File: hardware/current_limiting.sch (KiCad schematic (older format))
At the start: 3 parts, among them U7 MT9700

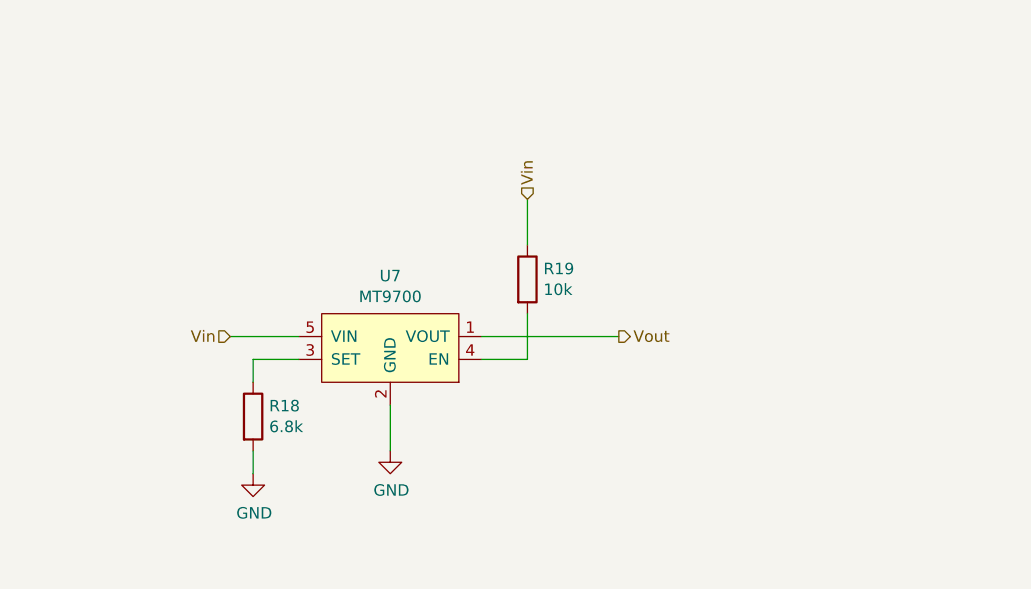
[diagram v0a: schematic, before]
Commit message: Changed to pure-serial topology. Changed to beefier mcu.
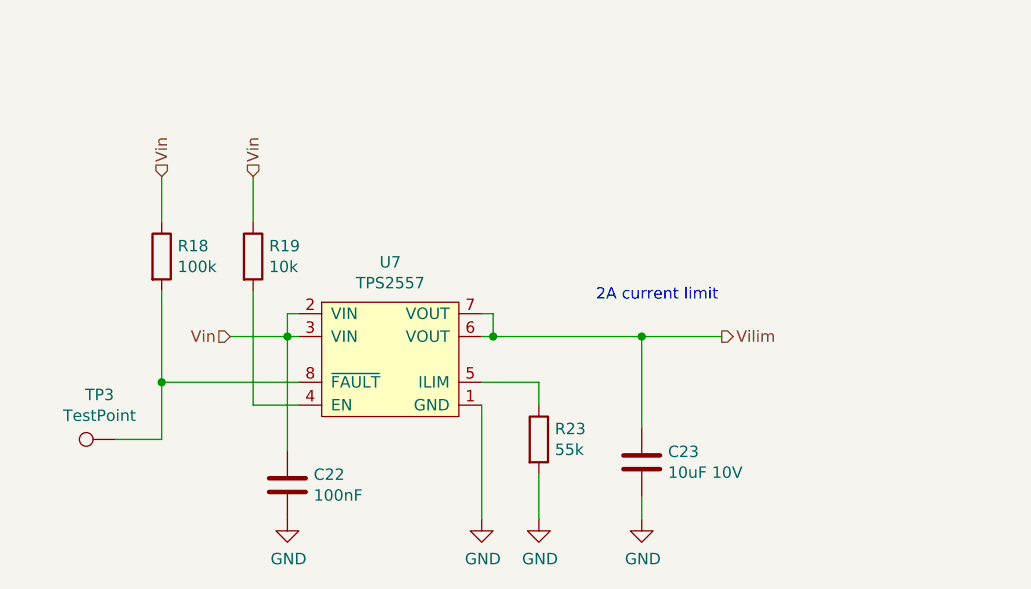
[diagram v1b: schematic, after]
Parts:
- removed U7: MT9700, Package_TO_SOT_SMD:SOT-23-5_HandSoldering, symbol pi-supercap-ups:MT9700
- added C22: 100nF, symbol Device:C
- added C23: 10uF 10V, symbol Device:C
- added R23: 55k, Resistor_SMD:R_0603_1608Metric_Pad1.05x0.95mm_HandSolder, symbol Device:R
- added TP3: TestPoint, symbol Connector:TestPoint
- added U7: TPS2557, symbol pi-supercap-ups:TPS2557
- R18: value 6.8k -> 100k
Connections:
- net GND: now also C22.2, C23.2, R23.2, U7.1 (GND); no longer R18.2
- net Vin: now also R18.1, C22.1, U7.2 (VIN), U7.3 (VIN)
- net at R19.2: now also U7.4 (EN)
- new net: R18.2, TP3.1, U7.8 (~FAULT)
- new net: R23.1, U7.5 (ILIM)
- new net Vilim: C23.1, U7.6 (VOUT), U7.7 (VOUT)
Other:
- note added: "2A current limit"
- moved on the sheet: R18, R19
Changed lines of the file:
@@
-EESchema Schematic File Version 4
+EESchema Schematic File Version 5
 LIBS:pi-supercap-ups-cache
-EELAYER 26 0
+EELAYER 30 0
 EELAYER END
 $Descr A4 11693 8268
 encoding utf-8
-Sheet 8 8
+Sheet 7 8
 Title ""
 Date ""
@@
 Comment4 ""
 $EndDescr
-$Comp
-L pi-supercap-ups:MT9700 U7
-U 1 1 5CA93FCA
-P 3000 2050
-F 0 "U7" H 3000 2365 50  0000 C CNN
-F 1 "MT9700" H 3000 2274 50  0000 C CNN
-F 2 "Package_TO_SOT_SMD:SOT-23-5_HandSoldering" H 3000 2250 50  0001 C CNN
-F 3 "" H 3000 2250 50  0001 C CNN
-	1    3000 2050
-	1    0    0    -1
-$EndComp
 Text HLabel 2300 2000 0    50   Input ~ 0
 Vin
-Text HLabel 4000 2000 2    50   Output ~ 0
-Vout
+Text HLabel 4450 2000 2    50   Output ~ 0
+Vilim
 $Comp
 L Device:R R18
 U 1 1 5CA94123
-P 2400 2350
-F 0 "R18" H 2470 2396 50  0000 L CNN
-F 1 "6.8k" H 2470 2305 50  0000 L CNN
-F 2 "Resistor_SMD:R_0603_1608Metric_Pad1.05x0.95mm_HandSolder" V 2330 2350 50  0001 C CNN
-F 3 "~" H 2400 2350 50  0001 C CNN
-	1    2400 2350
-	1    0    0    -1
-$EndComp
-Wire Wire Line
-	2400 2200 2400 2100
-Wire Wire Line
-	2400 2100 2600 2100
-Wire Wire Line
-	3400 2000 4000 2000
+P 2000 1650
+F 0 "R18" H 2070 1696 50  0000 L CNN
+F 1 "100k" H 2070 1605 50  0000 L CNN
+F 2 "Resistor_SMD:R_0603_1608Metric_Pad1.05x0.95mm_HandSolder" V 1930 1650 50  0001 C CNN
+F 3 "~" H 2000 1650 50  0001 C CNN
+	1    2000 1650
+	1    0    0    -1
+$EndComp
+Wire Wire Line
+	3400 2000 3450 2000
 $Comp
 L power:GND #PWR048
 U 1 1 5CA94273
-P 3000 2500
-F 0 "#PWR048" H 3000 2250 50  0001 C CNN
-F 1 "GND" H 3005 2327 50  0000 C CNN
-F 2 "" H 3000 2500 50  0001 C CNN
-F 3 "" H 3000 2500 50  0001 C CNN
-	1    3000 2500
-	1    0    0    -1
-$EndComp
-Wire Wire Line
-	3000 2500 3000 2300
+P 3400 2800
+F 0 "#PWR048" H 3400 2550 50  0001 C CNN
+F 1 "GND" H 3405 2627 50  0000 C CNN
+F 2 "" H 3400 2800 50  0001 C CNN
+F 3 "" H 3400 2800 50  0001 C CNN
+	1    3400 2800
+	1    0    0    -1
+$EndComp
+Wire Wire Line
+	3400 2800 3400 2300
 $Comp
 L Device:R R19
 U 1 1 5CA942F1
-P 3600 1750
-F 0 "R19" H 3670 1796 50  0000 L CNN
-F 1 "10k" H 3670 1705 50  0000 L CNN
-F 2 "Resistor_SMD:R_0603_1608Metric_Pad1.05x0.95mm_HandSolder" V 3530 1750 50  0001 C CNN
-F 3 "~" H 3600 1750 50  0001 C CNN
-	1    3600 1750
-	1    0    0    -1
-$EndComp
-Wire Wire Line
-	3400 2100 3600 2100
-Wire Wire Line
-	3600 2100 3600 1900
-Wire Wire Line
-	3600 1400 3600 1600
-Text HLabel 3600 1400 1    50   Input ~ 0
+P 2400 1650
+F 0 "R19" H 2470 1696 50  0000 L CNN
+F 1 "10k" H 2470 1605 50  0000 L CNN
+F 2 "Resistor_SMD:R_0603_1608Metric_Pad1.05x0.95mm_HandSolder" V 2330 1650 50  0001 C CNN
+F 3 "~" H 2400 1650 50  0001 C CNN
+	1    2400 1650
+	1    0    0    -1
+$EndComp
+Wire Wire Line
+	2400 1300 2400 1500
+Wire Wire Line
+	2300 2000 2550 2000
+Text HLabel 2400 1300 1    50   Input ~ 0
 Vin
-Wire Wire Line
-	2300 2000 2600 2000
-$Comp
-L power:GND #PWR047
-U 1 1 5CAAC9F8
-P 2400 2600
-F 0 "#PWR047" H 2400 2350 50  0001 C CNN
-F 1 "GND" H 2405 2427 50  0000 C CNN
-F 2 "" H 2400 2600 50  0001 C CNN
-F 3 "" H 2400 2600 50  0001 C CNN
-	1    2400 2600
-	1    0    0    -1
-$EndComp
-Wire Wire Line
-	2400 2600 2400 2500
+Text HLabel 2000 1300 1    50   Input ~ 0
+Vin
+Wire Wire Line
+	2000 1300 2000 1500
+$Comp
+L Connector:TestPoint TP3
+U 1 1 5D5092EF
+P 1800 2450
+F 0 "TP3" V 1995 2522 50  0000 C CNN
+F 1 "TestPoint" V 1904 2522 50  0000 C CNN
+F 2 "" H 2000 2450 50  0001 C CNN
+F 3 "~" H 2000 2450 50  0001 C CNN
+	1    1800 2450
+	0    -1   -1   0
+$EndComp
+Wire Wire Line
+	1800 2450 2000 2450
+Wire Wire Line
+	2000 2450 2000 2200
+Text Notes 3900 1850 0    50   ~ 0
+2A current limit
+$Comp
+L Device:C C22
+U 1 1 5D50C9A4
+P 2550 2650
+F 0 "C22" H 2665 2696 50  0000 L CNN
+F 1 "100nF" H 2665 2605 50  0000 L CNN
+F 2 "" H 2588 2500 50  0001 C CNN
+F 3 "~" H 2550 2650 50  0001 C CNN
+	1    2550 2650
+	1    0    0    -1
+$EndComp
+$Comp
+L Device:C C23
+U 1 1 5D50F4B5
+P 4100 2550
+F 0 "C23" H 4215 2596 50  0000 L CNN
+F 1 "10uF 10V" H 4215 2505 50  0000 L CNN
+F 2 "" H 4138 2400 50  0001 C CNN
+F 3 "~" H 4100 2550 50  0001 C CNN
+	1    4100 2550
+	1    0    0    -1
+$EndComp
+Connection ~ 2550 2000
+Wire Wire Line
+	2550 2000 2600 2000
+$Comp
+L power:GND #PWR0111
+U 1 1 5D5101D8
+P 2550 2800
+F 0 "#PWR0111" H 2550 2550 50  0001 C CNN
+F 1 "GND" H 2555 2627 50  0000 C CNN
+F 2 "" H 2550 2800 50  0001 C CNN
+F 3 "" H 2550 2800 50  0001 C CNN
+	1    2550 2800
+	1    0    0    -1
+$EndComp
+$Comp
+L power:GND #PWR0112
+U 1 1 5D510451
+P 4100 2800
+F 0 "#PWR0112" H 4100 2550 50  0001 C CNN
+F 1 "GND" H 4105 2627 50  0000 C CNN
+F 2 "" H 4100 2800 50  0001 C CNN
+F 3 "" H 4100 2800 50  0001 C CNN
+	1    4100 2800
+	1    0    0    -1
+$EndComp
+Wire Wire Line
+	4100 2800 4100 2700
+$Comp
+L pi-supercap-ups:TPS2557 U7
+U 1 1 5D5343A5
+P 3050 2100
+F 0 "U7" H 3000 2525 50  0000 C CNN
+F 1 "TPS2557" H 3000 2434 50  0000 C CNN
+F 2 "" H 3050 2300 50  0001 C CNN
+F 3 "" H 3050 2300 50  0001 C CNN
+	1    3050 2100
+	1    0    0    -1
+$EndComp
+Wire Wire Line
+	2600 1900 2550 1900
+Wire Wire Line
+	2550 1900 2550 2000
+Wire Wire Line
+	3400 1900 3450 1900
+Wire Wire Line
+	3450 1900 3450 2000
+Connection ~ 3450 2000
+Wire Wire Line
+	2400 1800 2400 2300
+Wire Wire Line
+	2400 2300 2600 2300
+Connection ~ 2000 2200
+Wire Wire Line
+	2000 1800 2000 2200
+Wire Wire Line
+	2000 2200 2600 2200
+Wire Wire Line
+	2550 2500 2550 2000
+Wire Wire Line
+	4100 2000 4100 2400
+Connection ~ 4100 2000
+Wire Wire Line
+	4100 2000 4450 2000
+Wire Wire Line
+	3450 2000 4100 2000
+$Comp
+L Device:R R23
+U 1 1 5D537A8C
+P 3650 2450
+F 0 "R23" H 3720 2496 50  0000 L CNN
+F 1 "55k" H 3720 2405 50  0000 L CNN
+F 2 "Resistor_SMD:R_0603_1608Metric_Pad1.05x0.95mm_HandSolder" V 3580 2450 50  0001 C CNN
+F 3 "~" H 3650 2450 50  0001 C CNN
+	1    3650 2450
+	1    0    0    -1
+$EndComp
+Wire Wire Line
+	3400 2200 3650 2200
+Wire Wire Line
+	3650 2200 3650 2300
+$Comp
+L power:GND #PWR0113
+U 1 1 5D53801C
+P 3650 2800
+F 0 "#PWR0113" H 3650 2550 50  0001 C CNN
+F 1 "GND" H 3655 2627 50  0000 C CNN
+F 2 "" H 3650 2800 50  0001 C CNN
+F 3 "" H 3650 2800 50  0001 C CNN
+	1    3650 2800
+	1    0    0    -1
+$EndComp
+Wire Wire Line
+	3650 2800 3650 2600
 $EndSCHEMATC

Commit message: Layout partially done before change of plans
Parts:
- removed TP3: TestPoint, symbol Connector:TestPoint
- removed U7: TPS2557, symbol pi-supercap-ups:TPS2557
- added C20, C21: 10uF 10V, Capacitor_SMD:C_0603_1608Metric_Pad1.05x0.95mm_HandSolder, symbol Device:C
- added U6, U7: MT9700, Package_TO_SOT_SMD:SOT-23-5_HandSoldering, symbol pi-supercap-ups:MT9700
- C22: value 100nF -> 10uF 10V; footprint (none) -> Capacitor_SMD:C_0603_1608Metric_Pad1.05x0.95mm_HandSolder
- C23: footprint (none) -> Capacitor_SMD:C_0603_1608Metric_Pad1.05x0.95mm_HandSolder
- R18: value 100k -> 4.53k
- R23: value 55k -> 4.53k
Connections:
- net GND: now also R18.2, C20.2, C21.2, U6.2 (GND), U7.2 (GND)
- net Vilim: now also C22.1, U6.1 (VOUT), U7.1 (VOUT)
- net Vin: now also C20.1, C21.1, U6.5 (VIN), U7.5 (VIN); no longer C22.1, R18.1
- net at R19.2: now also U6.4 (EN), U7.4 (EN)
- net at R23.1: now also U7.3 (SET)
- new net: R18.1, U6.3 (SET)
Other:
- note added: "2*1.5A current limit"
- note removed: "2A current limit"
- moved on the sheet: C23, R19, R23

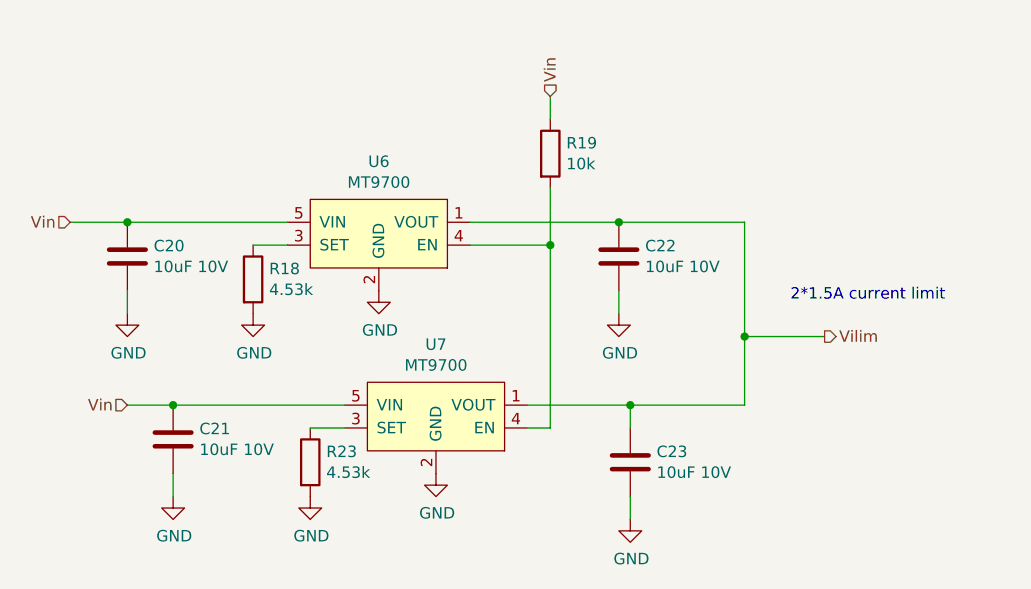
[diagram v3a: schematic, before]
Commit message: Add ENIN trace to the PCB. Change input voltage dividers for 1.1V ref.
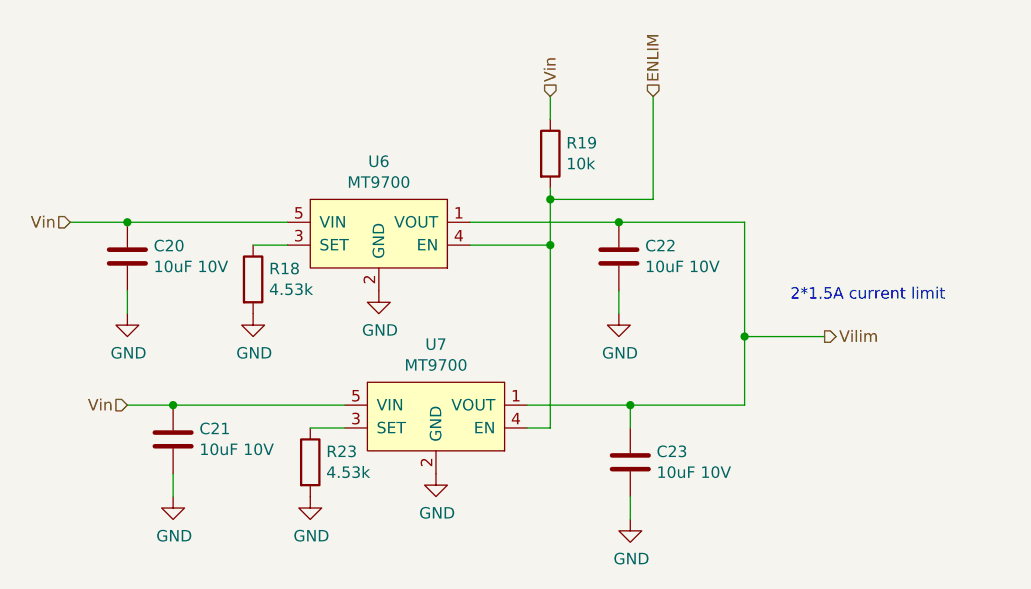
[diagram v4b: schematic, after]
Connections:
- net ENLIM: now reaches R19.2, U6.4 (EN), U7.4 (EN)
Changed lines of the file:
@@
 Connection ~ 3700 1600
 Wire Wire Line
-	3700 1350 3700 1600
+	3700 1350 3700 1400
 Wire Wire Line
 	4550 1500 4550 2000
@@
 	1    0    0    -1
 $EndComp
+Text HLabel 4150 950  1    50   Input ~ 0
+ENLIM
+Wire Wire Line
+	4150 950  4150 1400
+Wire Wire Line
+	4150 1400 3700 1400
+Connection ~ 3700 1400
+Wire Wire Line
+	3700 1400 3700 1600
 $EndSCHEMATC

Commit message: Fix component values etc
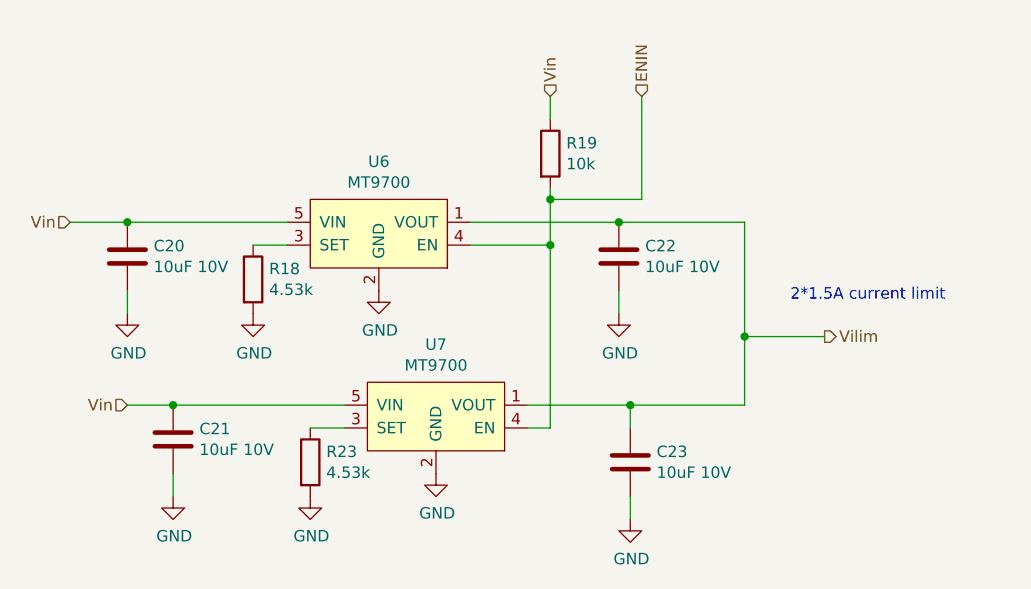
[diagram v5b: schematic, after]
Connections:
- net ENLIM renamed ENIN
